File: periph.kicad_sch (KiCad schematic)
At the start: 43 parts, among them J10 BOOTLOADER_UART, J11 Button, J12 Load, J6 ARM_JTAG, J7 USB_B_MINI, J8 Magnet, J9 iButton, Q1 IRF740, Q2 BCX56, Q3 AO3400A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

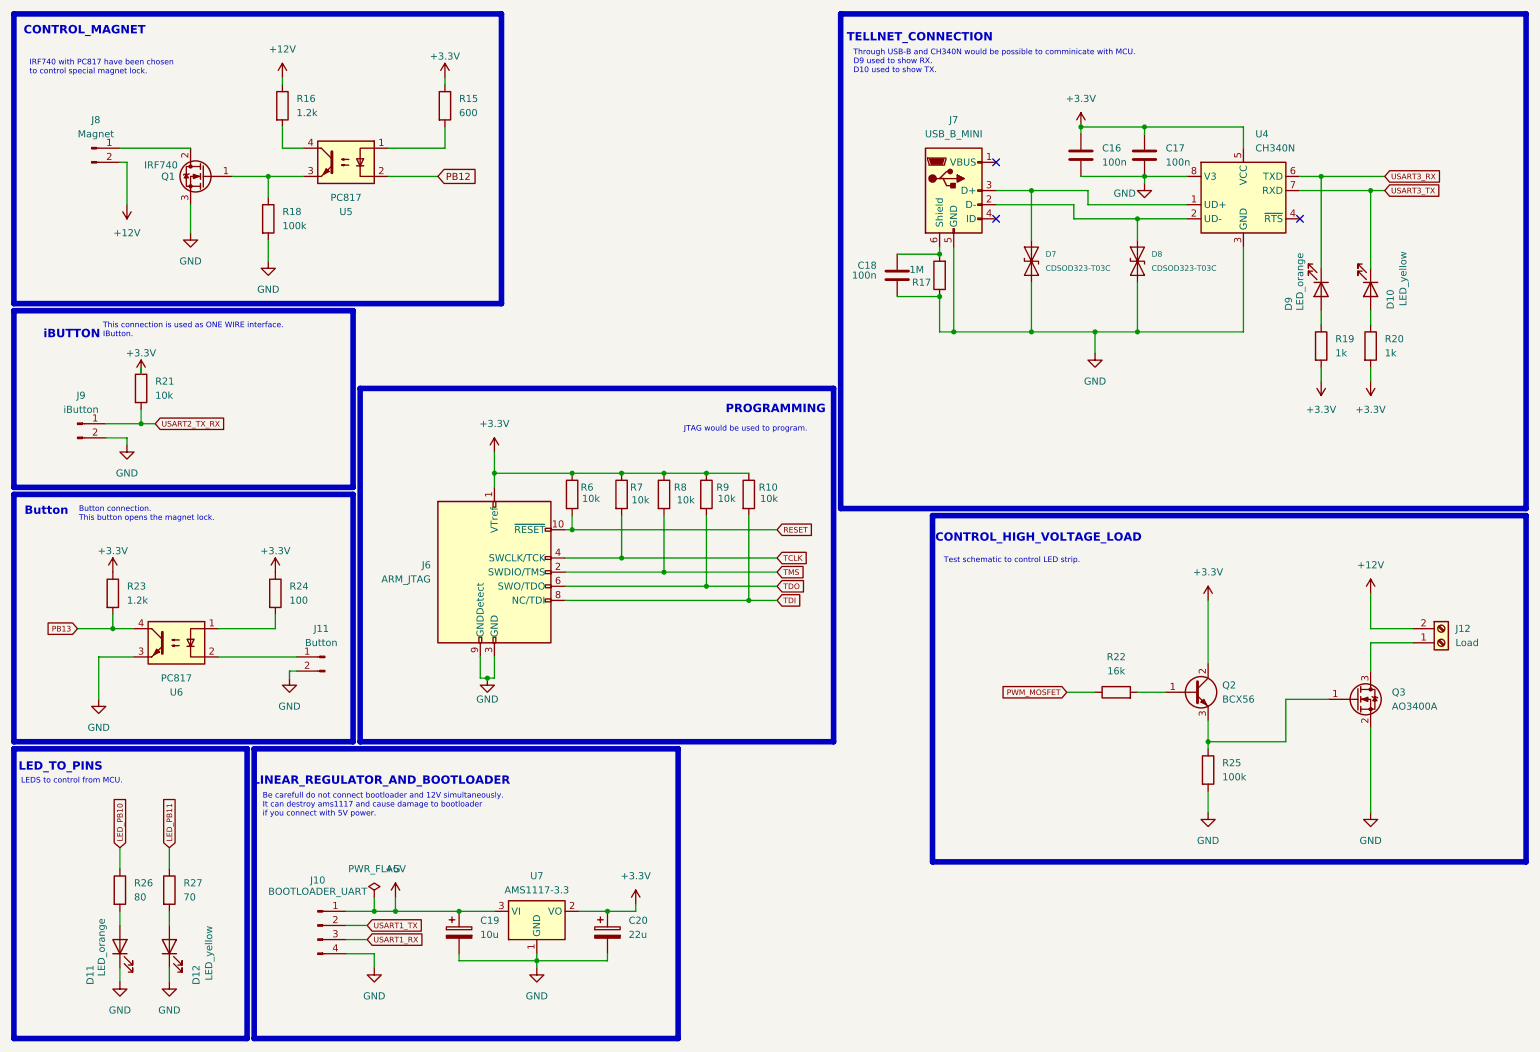
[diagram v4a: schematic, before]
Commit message: CH340N has been added. Previous version was wrong. Pin V3 was wrong placed and was connected to GND
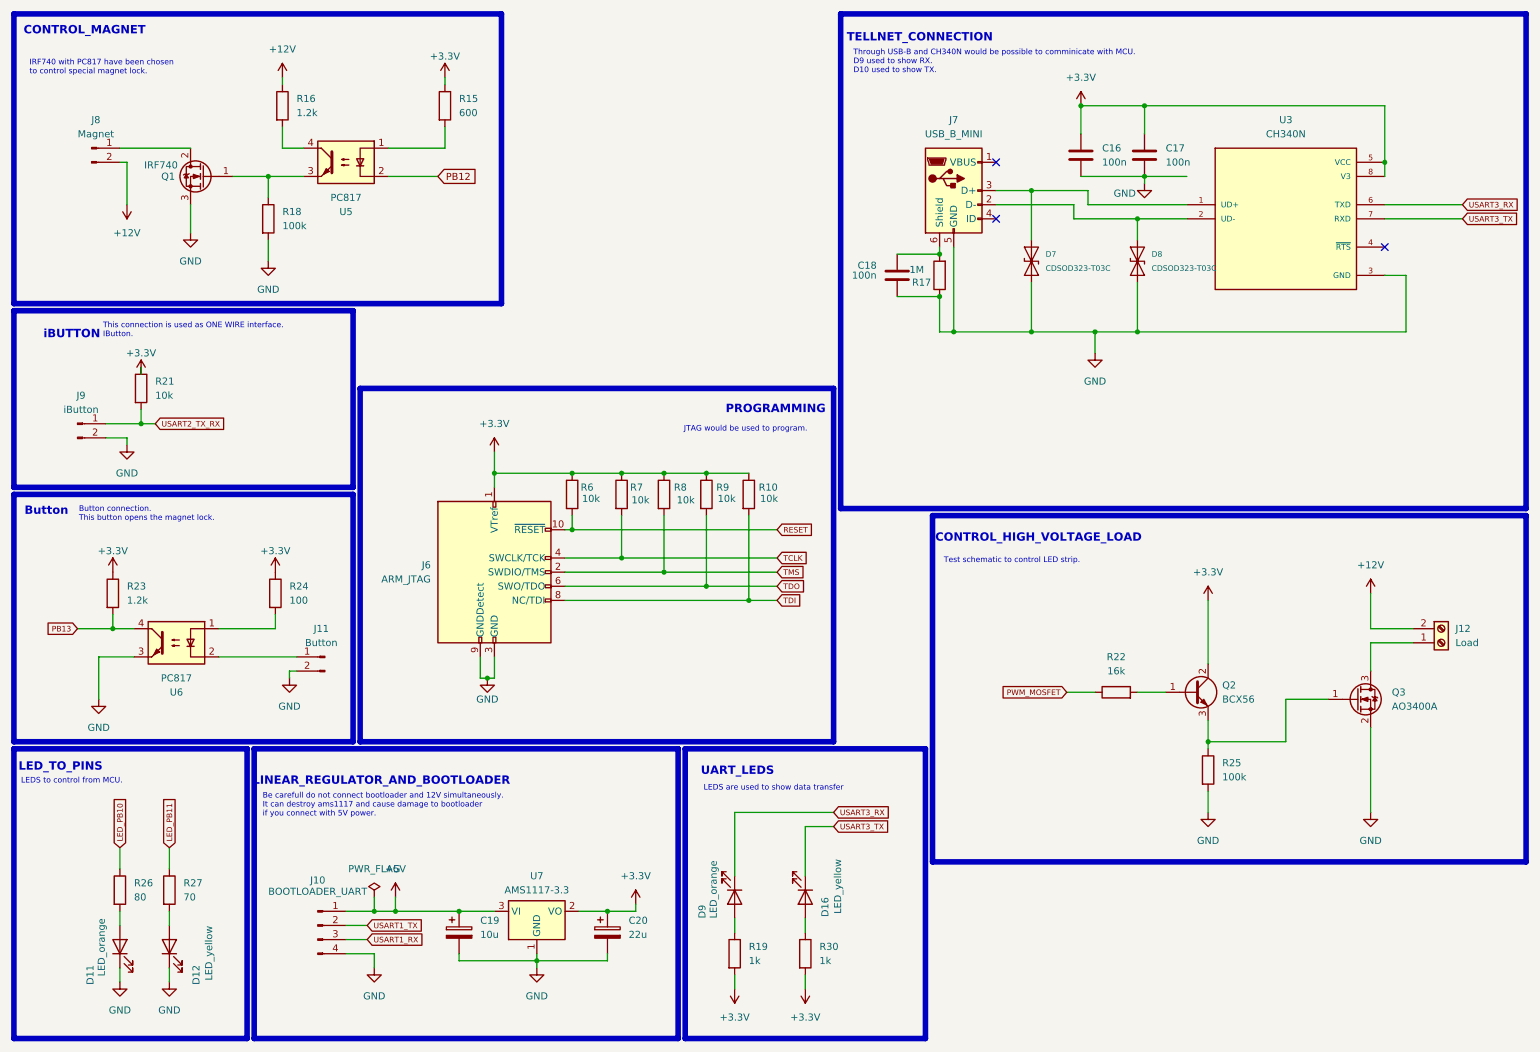
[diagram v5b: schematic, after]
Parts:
- removed D10: LED_yellow, LED_SMD:LED_1206_3216Metric, symbol Device:LED
- removed R20: 1k, Resistor_SMD:R_1206_3216Metric_Pad1.30x1.75mm_HandSolder, symbol Device:R
- removed U4: CH340N, Package_SO:SOP-8_3.9x4.9mm_P1.27mm, symbol Interface_USB:CH340N
- added D16: LED_yellow, LED_SMD:LED_1206_3216Metric, symbol Device:LED
- added R30: 1k, Resistor_SMD:R_1206_3216Metric_Pad1.30x1.75mm_HandSolder, symbol Device:R
- added U3: CH340N, CH340N:SOIC127P600X160-8N, symbol CH340N:CH340N
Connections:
- net +3.3V: now also R30.2, U3.5 (VCC), U3.8 (V3)
- net GND: now also U3.3 (GND)
- net USART3_RX: now also U3.6 (TXD)
- net USART3_TX: now also D16.1 (K), U3.7 (RXD)
- net at D8.2 (A2), J7.2 (D-): now also U3.2 (UD-)
- net at D7.2 (A2), J7.3 (D+): now also U3.1 (UD+)
- new net: D16.2 (A), R30.1
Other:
- note added: "LEDS are used to show data transfer"
- note added: "UART_LEDS"
- company: (none) -> HOMEMADE
- title: (none) -> ProgrammLockControl(Peripheria)
- moved on the sheet: D9, R19

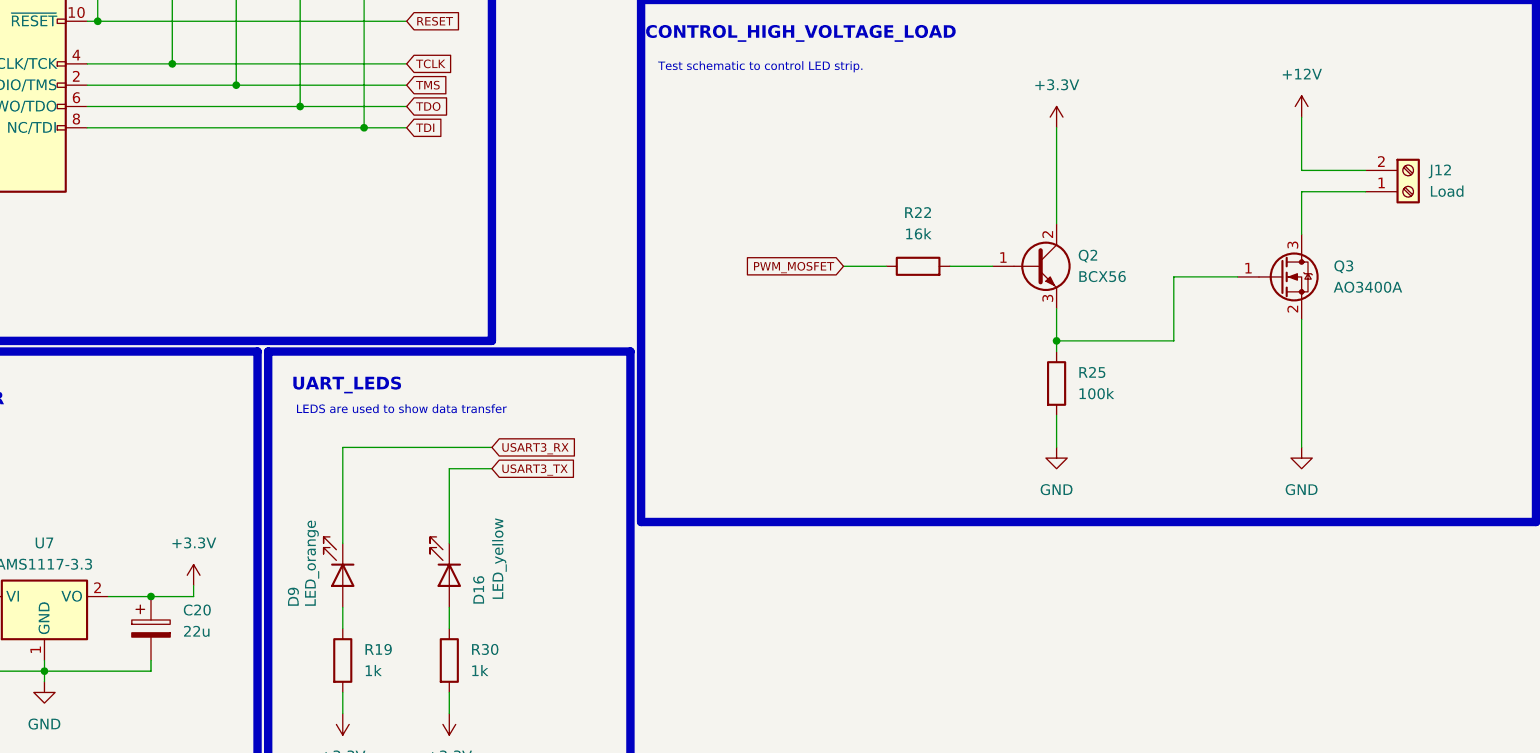
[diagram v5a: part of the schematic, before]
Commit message: Shottky diod has been added to provide protection for AMS1117-3.3
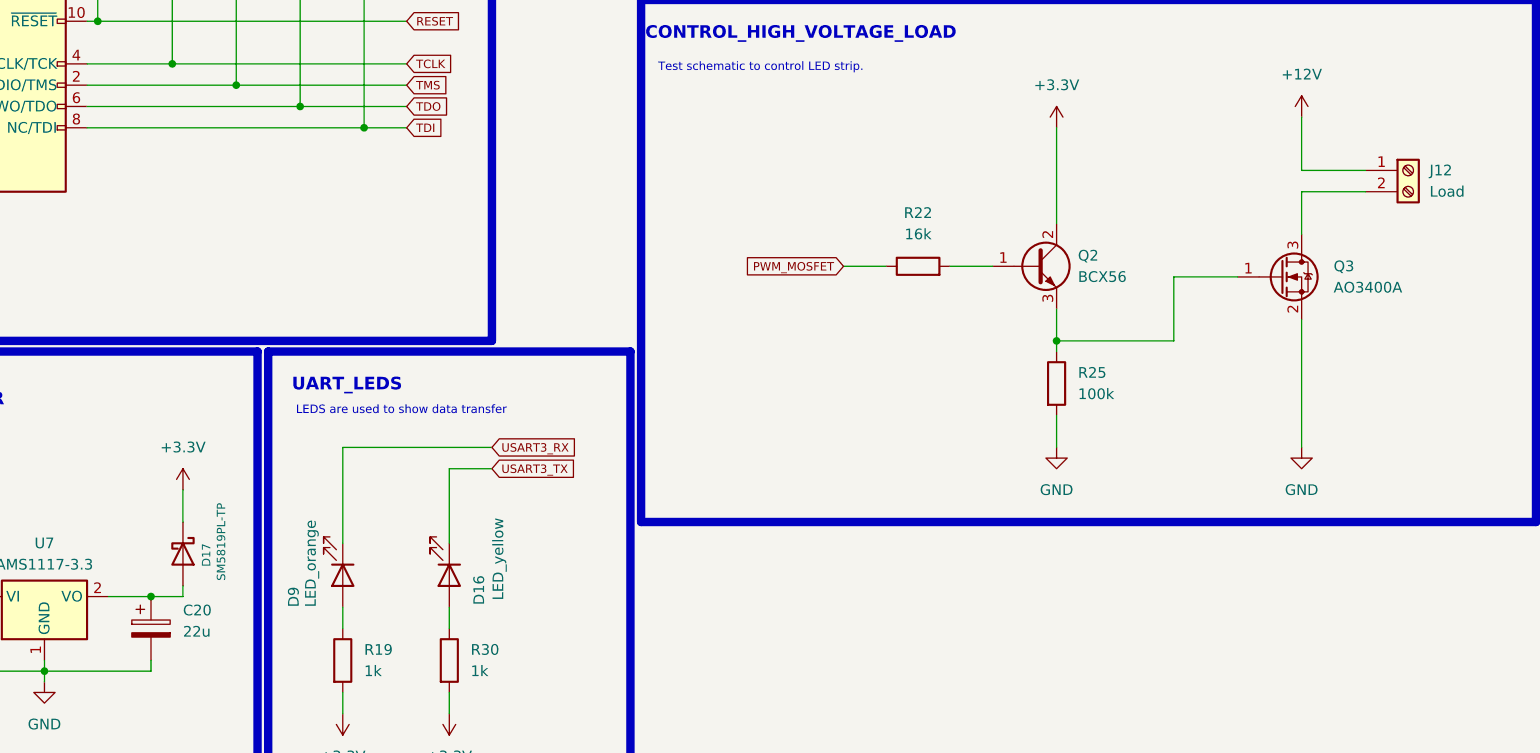
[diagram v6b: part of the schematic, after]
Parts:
- added D17: SM5819PL-TP, Diode_SMD:D_SOD-123F, symbol Diode:1N5822
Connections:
- net +12V: now also J12.1 (Pin_1); no longer J12.2 (Pin_1)
- net +3.3V: now also D17.1 (K); no longer C20.1, U7.2 (VO)
- net at Q3.3 (D): now also J12.2 (Pin_2); no longer J12.1 (Pin_2)
- new net: C20.1, D17.2 (A), U7.2 (VO)
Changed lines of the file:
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@@
 	(wire
 		(pts
-			(xy 119.38 173.99) (xy 124.46 173.99)
+			(xy 119.38 173.99) (xy 123.19 173.99)
 		)
 		(stroke
@@
 	(wire
 		(pts
+			(xy 123.19 172.72) (xy 123.19 173.99)
+		)
+		(stroke
+			(width 0)
+			(type default)
+		)
+	)
+	(wire
+		(pts
 			(xy 119.38 181.61) (xy 119.38 182.88)
 		)
@@
 	(wire
 		(pts
-			(xy 124.46 172.72) (xy 124.46 173.99)
+			(xy 123.19 161.29) (xy 123.19 165.1)
 		)
 		(stroke
@@
 				(path "/664afda1-d053-4a3e-94ea-5cfb2e9bf32c/ffa69088-c12a-4df7-8c5b-b320b479fef0"
 					(reference "#PWR048")
+					(unit 1)
+				)
+			)
+		)
+	)
+	(symbol
+		(lib_id "Diode:1N5822")
+		(at 123.19 168.91 270)
+		(unit 1)
+		(exclude_from_sim no)
+		(in_bom yes)
+		(on_board yes)
+		(dnp no)
+		(property "Reference" "D17"
+			(at 125.984 167.64 0)
+			(effects
+				(font
+					(size 1 1)
+				)
+				(justify left)
+			)
+		)
+		(property "Value" "SM5819PL-TP"
+			(at 127.762 162.814 0)
+			(effects
+				(font
+					(size 1 1)
+				)
+				(justify left)
+			)
+		)
+		(property "Footprint" "Diode_SMD:D_SOD-123F"
+			(at 118.745 168.91 0)
+			(effects
+				(font
+					(size 1.27 1.27)
+				)
+				(hide yes)
+			)
+		)
+		(property "Datasheet" "http://www.vishay.com/docs/88526/1n5820.pdf"
+			(at 123.19 168.91 0)
+			(effects
+				(font
+					(size 1.27 1.27)
+				)
+				(hide yes)
+			)
+		)
+		(property "Description" "40V 3A Schottky Barrier Rectifier Diode, DO-201AD"
+			(at 123.19 168.91 0)
+			(effects
+				(font
+					(size 1.27 1.27)
+				)
+				(hide yes)
+			)
+		)
+		(pin "1"
+		)
+		(pin "2"
+		)
+		(instances
+			(project "stm32f103"
+				(path "/664afda1-d053-4a3e-94ea-5cfb2e9bf32c/ffa69088-c12a-4df7-8c5b-b320b479fef0"
+					(reference "D17")
 					(unit 1)
 				)
@@
 	(symbol
 		(lib_id "power:+3.3V")
-		(at 124.46 172.72 0)
+		(at 123.19 161.29 0)
 		(unit 1)
 		(exclude_from_sim no)
@@
 		(fields_autoplaced yes)
 		(property "Reference" "#PWR060"
-			(at 124.46 176.53 0)
+			(at 123.19 165.1 0)
 			(effects
 				(font
@@
 		)
 		(property "Value" "+3.3V"
-			(at 124.46 167.64 0)
+			(at 123.19 156.21 0)
 			(effects
 				(font
@@
 		)
 		(property "Footprint" ""
-			(at 124.46 172.72 0)
+			(at 123.19 161.29 0)
 			(effects
 				(font
@@
 		)
 		(property "Datasheet" ""
-			(at 124.46 172.72 0)
+			(at 123.19 161.29 0)
 			(effects
 				(font
@@
 		)
 		(property "Description" "Power symbol creates a global label with name \"+3.3V\""
-			(at 124.46 172.72 0)
-			(effects
-				(font
+			(at 123.19 161.29 0)
+			(effects
+				(font
